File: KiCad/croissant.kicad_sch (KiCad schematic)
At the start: 53 parts, among them J1 USB_C_Receptacle_PowerOnly_6P, Q1 NMOS, SW1 SW_SPDT, U1 NE556, U2 TL064

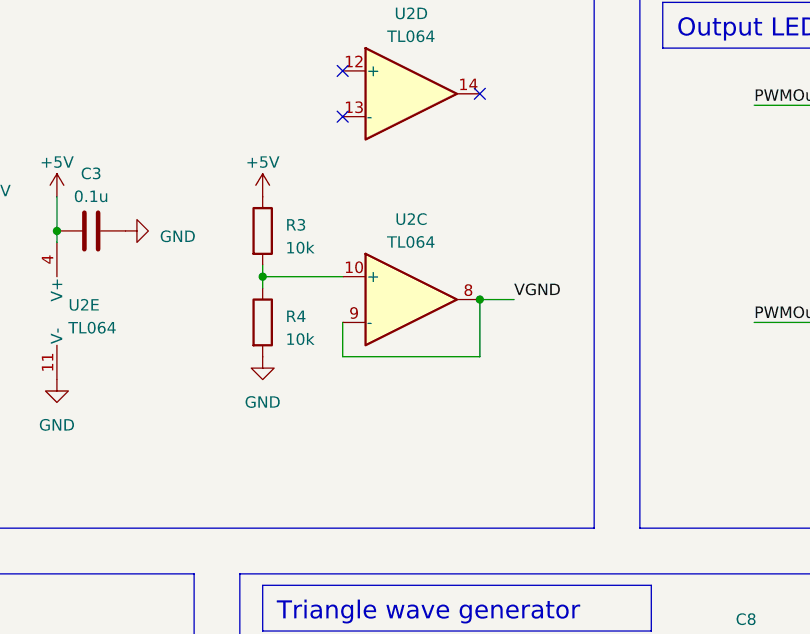
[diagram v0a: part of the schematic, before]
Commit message: Placed LEDs
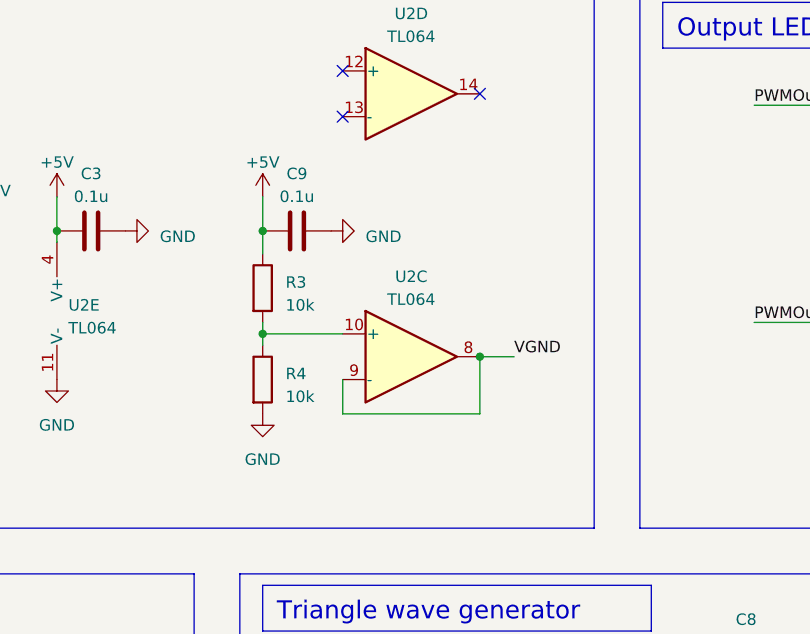
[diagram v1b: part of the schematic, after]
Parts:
- added C9: 0.1u, Capacitor_SMD:C_0603_1608Metric, symbol Device:C
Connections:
- net +5V: now also C9.1
- net GND: now also C9.2
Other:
- moved on the sheet: R3, R4, U2C
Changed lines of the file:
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@@
   (junction (at 63.5 132.08) (diameter 0) (color 0 0 0 0)
   )
-  (junction (at 133.35 66.04) (diameter 0) (color 0 0 0 0)
+  (junction (at 133.35 72.39) (diameter 0) (color 0 0 0 0)
   )
   (junction (at 261.62 105.41) (diameter 0) (color 0 0 0 0)
@@
   (junction (at 233.68 44.45) (diameter 0) (color 0 0 0 0)
   )
-  (junction (at 109.22 63.5) (diameter 0) (color 0 0 0 0)
+  (junction (at 109.22 69.85) (diameter 0) (color 0 0 0 0)
   )
   (junction (at 215.9 68.58) (diameter 0) (color 0 0 0 0)
@@
   )
   (junction (at 45.72 113.03) (diameter 0) (color 0 0 0 0)
+  )
+  (junction (at 109.22 58.42) (diameter 0) (color 0 0 0 0)
   )
   (junction (at 198.12 68.58) (diameter 0) (color 0 0 0 0)
@@
     (stroke (width 0) (type default))
   )
-  (wire (pts (xy 133.35 72.39) (xy 133.35 66.04))
+  (wire (pts (xy 133.35 78.74) (xy 133.35 72.39))
     (stroke (width 0) (type default))
   )
@@
     (stroke (width 0) (type default))
   )
-  (wire (pts (xy 109.22 63.5) (xy 118.11 63.5))
+  (wire (pts (xy 109.22 69.85) (xy 118.11 69.85))
     (stroke (width 0) (type default))
   )
@@
     (stroke (width 0) (type default))
   )
-  (wire (pts (xy 109.22 62.23) (xy 109.22 63.5))
+  (wire (pts (xy 109.22 58.42) (xy 109.22 54.61))
+    (stroke (width 0) (type default))
+  )
+  (wire (pts (xy 109.22 68.58) (xy 109.22 69.85))
     (stroke (width 0) (type default))
   )
@@
     (stroke (width 0) (type default))
   )
+  (wire (pts (xy 109.22 58.42) (xy 109.22 60.96))
+    (stroke (width 0) (type default))
+  )
   (wire (pts (xy 215.9 44.45) (xy 224.79 44.45))
     (stroke (width 0) (type default))
@@
     (stroke (width 0) (type default))
   )
-  (wire (pts (xy 109.22 63.5) (xy 109.22 64.77))
+  (wire (pts (xy 109.22 69.85) (xy 109.22 71.12))
     (stroke (width 0) (type default))
   )
@@
     (stroke (width 0) (type default))
   )
-  (wire (pts (xy 118.11 68.58) (xy 118.11 72.39))
+  (wire (pts (xy 118.11 74.93) (xy 118.11 78.74))
     (stroke (width 0) (type default))
   )
@@
     (stroke (width 0) (type default))
   )
-  (wire (pts (xy 118.11 72.39) (xy 133.35 72.39))
+  (wire (pts (xy 118.11 78.74) (xy 133.35 78.74))
     (stroke (width 0) (type default))
   )
@@
     (stroke (width 0) (type default))
   )
-  (wire (pts (xy 133.35 66.04) (xy 137.16 66.04))
+  (wire (pts (xy 133.35 72.39) (xy 137.16 72.39))
     (stroke (width 0) (type default))
   )
@@
     (effects (font (size 1.27 1.27)) (justify left bottom))
   )
-  (label "VGND" (at 137.16 66.04 0) (fields_autoplaced)
+  (label "VGND" (at 137.16 72.39 0) (fields_autoplaced)
     (effects (font (size 1.27 1.27)) (justify left bottom))
   )
@@
     )
   )
-  (symbol (lib_id "Device:R") (at 109.22 58.42 0) (unit 1)
-    (in_bom yes) (on_board yes) (dnp no) (fields_autoplaced)
-    (property "Reference" "R3" (at 111.76 57.785 0)
-      (effects (font (size 1.27 1.27)) (justify left))
-    )
-    (property "Value" "10k" (at 111.76 60.325 0)
-      (effects (font (size 1.27 1.27)) (justify left))
-    )
-    (property "Footprint" "Resistor_SMD:R_0603_1608Metric" (at 107.442 58.42 90)
-      (effects (font (size 1.27 1.27)) hide)
-    )
-    (property "Datasheet" "~" (at 109.22 58.42 0)
+  (symbol (lib_id "Device:R") (at 109.22 64.77 0) (unit 1)
+    (in_bom yes) (on_board yes) (dnp no) (fields_autoplaced)
+    (property "Reference" "R3" (at 111.76 64.135 0)
+      (effects (font (size 1.27 1.27)) (justify left))
+    )
+    (property "Value" "10k" (at 111.76 66.675 0)
+      (effects (font (size 1.27 1.27)) (justify left))
+    )
+    (property "Footprint" "Resistor_SMD:R_0603_1608Metric" (at 107.442 64.77 90)
+      (effects (font (size 1.27 1.27)) hide)
+    )
+    (property "Datasheet" "~" (at 109.22 64.77 0)
       (effects (font (size 1.27 1.27)) hide)
     )
@@
     )
   )
-  (symbol (lib_id "Device:R") (at 109.22 68.58 0) (unit 1)
-    (in_bom yes) (on_board yes) (dnp no) (fields_autoplaced)
-    (property "Reference" "R4" (at 111.76 67.945 0)
-      (effects (font (size 1.27 1.27)) (justify left))
-    )
-    (property "Value" "10k" (at 111.76 70.485 0)
-      (effects (font (size 1.27 1.27)) (justify left))
-    )
-    (property "Footprint" "Resistor_SMD:R_0603_1608Metric" (at 107.442 68.58 90)
-      (effects (font (size 1.27 1.27)) hide)
-    )
-    (property "Datasheet" "~" (at 109.22 68.58 0)
+  (symbol (lib_id "Device:R") (at 109.22 74.93 0) (unit 1)
+    (in_bom yes) (on_board yes) (dnp no) (fields_autoplaced)
+    (property "Reference" "R4" (at 111.76 74.295 0)
+      (effects (font (size 1.27 1.27)) (justify left))
+    )
+    (property "Value" "10k" (at 111.76 76.835 0)
+      (effects (font (size 1.27 1.27)) (justify left))
+    )
+    (property "Footprint" "Resistor_SMD:R_0603_1608Metric" (at 107.442 74.93 90)
+      (effects (font (size 1.27 1.27)) hide)
+    )
+    (property "Datasheet" "~" (at 109.22 74.93 0)
       (effects (font (size 1.27 1.27)) hide)
     )
@@
     )
   )
-  (symbol (lib_id "power:GND") (at 109.22 72.39 0) (unit 1)
-    (in_bom yes) (on_board yes) (dnp no) (fields_autoplaced)
-    (property "Reference" "#PWR016" (at 109.22 78.74 0)
-      (effects (font (size 1.27 1.27)) hide)
-    )
-    (property "Value" "GND" (at 109.22 77.47 0)
-      (effects (font (size 1.27 1.27)))
-    )
-    (property "Footprint" "" (at 109.22 72.39 0)
-      (effects (font (size 1.27 1.27)) hide)
-    )
-    (property "Datasheet" "" (at 109.22 72.39 0)
+  (symbol (lib_id "power:GND") (at 109.22 78.74 0) (unit 1)
+    (in_bom yes) (on_board yes) (dnp no) (fields_autoplaced)
+    (property "Reference" "#PWR016" (at 109.22 85.09 0)
+      (effects (font (size 1.27 1.27)) hide)
+    )
+    (property "Value" "GND" (at 109.22 83.82 0)
+      (effects (font (size 1.27 1.27)))
+    )
+    (property "Footprint" "" (at 109.22 78.74 0)
+      (effects (font (size 1.27 1.27)) hide)
+    )
+    (property "Datasheet" "" (at 109.22 78.74 0)
       (effects (font (size 1.27 1.27)) hide)
     )
@@
     )
   )
+  (symbol (lib_id "Device:C") (at 113.03 58.42 90) (unit 1)
+    (in_bom yes) (on_board yes) (dnp no) (fields_autoplaced)
+    (property "Reference" "C9" (at 113.03 52.07 90)
+      (effects (font (size 1.27 1.27)))
+    )
+    (property "Value" "0.1u" (at 113.03 54.61 90)
+      (effects (font (size 1.27 1.27)))
+    )
+    (property "Footprint" "Capacitor_SMD:C_0603_1608Metric" (at 116.84 57.4548 0)
+      (effects (font (size 1.27 1.27)) hide)
+    )
+    (property "Datasheet" "~" (at 113.03 58.42 0)
+      (effects (font (size 1.27 1.27)) hide)
+    )
+    (pin "1")
+    (pin "2")
+    (instances
+      (project "croissant"
+        (path "/9d4c4425-9345-4751-a711-72e95f2cc96d"
+          (reference "C9") (unit 1)
+        )
+      )
+    )
+  )
   (symbol (lib_id "power:PWR_FLAG") (at 71.12 53.34 0) (unit 1)
     (in_bom yes) (on_board yes) (dnp no) (fields_autoplaced)
@@
     )
   )
-  (symbol (lib_id "Amplifier_Operational:TL064") (at 125.73 66.04 0) (unit 3)
-    (in_bom yes) (on_board yes) (dnp no) (fields_autoplaced)
-    (property "Reference" "U2" (at 125.73 57.15 0)
-      (effects (font (size 1.27 1.27)))
-    )
-    (property "Value" "TL064" (at 125.73 59.69 0)
-      (effects (font (size 1.27 1.27)))
-    )
-    (property "Footprint" "Package_SO:SOIC-14_3.9x8.7mm_P1.27mm" (at 124.46 63.5 0)
-      (effects (font (size 1.27 1.27)) hide)
-    )
-    (property "Datasheet" "http://www.ti.com/lit/ds/symlink/tl061.pdf" (at 127 60.96 0)
+  (symbol (lib_id "Amplifier_Operational:TL064") (at 125.73 72.39 0) (unit 3)
+    (in_bom yes) (on_board yes) (dnp no) (fields_autoplaced)
+    (property "Reference" "U2" (at 125.73 63.5 0)
+      (effects (font (size 1.27 1.27)))
+    )
+    (property "Value" "TL064" (at 125.73 66.04 0)
+      (effects (font (size 1.27 1.27)))
+    )
+    (property "Footprint" "Package_SO:SOIC-14_3.9x8.7mm_P1.27mm" (at 124.46 69.85 0)
+      (effects (font (size 1.27 1.27)) hide)
+    )
+    (property "Datasheet" "http://www.ti.com/lit/ds/symlink/tl061.pdf" (at 127 67.31 0)
       (effects (font (size 1.27 1.27)) hide)
     )
@@
         )
       )
+    )
+  )
+  (symbol (lib_id "power:GND") (at 116.84 58.42 90) (unit 1)
+    (in_bom yes) (on_board yes) (dnp no) (fields_autoplaced)
+    (property "Reference" "#PWR039" (at 123.19 58.42 0)
+      (effects (font (size 1.27 1.27)) hide)
+    )
+    (property "Value" "GND" (at 120.65 59.055 90)
+      (effects (font (size 1.27 1.27)) (justify right))
+    )
+    (property "Footprint" "" (at 116.84 58.42 0)
+      (effects (font (size 1.27 1.27)) hide)
+    )
+    (property "Datasheet" "" (at 116.84 58.42 0)
+      (effects (font (size 1.27 1.27)) hide)
+    )
+    (pin "1")
+    (instances
+      (project "croissant"
+        (path "/9d4c4425-9345-4751-a711-72e95f2cc96d"
+          (reference "#PWR039") (unit 1)
+        )
+      )

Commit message: Fix LEDs silkscreen
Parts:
- D1, D10, D11, D12, D13, D14, D15, D2, D3, D4, D5, D6, D7, D8, D9: footprint LED_SMD:LED_0603_1608Metric -> croissant:LED_0603_NOSILK
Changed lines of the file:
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@@
       (effects (font (size 1.27 1.27)) (justify right))
     )
-    (property "Footprint" "LED_SMD:LED_0603_1608Metric" (at 215.9 80.01 0)
+    (property "Footprint" "croissant:LED_0603_NOSILK" (at 215.9 80.01 0)
       (effects (font (size 1.27 1.27)) hide)
     )
@@
       (effects (font (size 1.27 1.27)) (justify right))
     )
-    (property "Footprint" "LED_SMD:LED_0603_1608Metric" (at 215.9 55.88 0)
+    (property "Footprint" "croissant:LED_0603_NOSILK" (at 215.9 55.88 0)
       (effects (font (size 1.27 1.27)) hide)
     )
@@
       (effects (font (size 1.27 1.27)) (justify right))
     )
-    (property "Footprint" "LED_SMD:LED_0603_1608Metric" (at 198.12 55.88 0)
+    (property "Footprint" "croissant:LED_0603_NOSILK" (at 198.12 55.88 0)
       (effects (font (size 1.27 1.27)) hide)
     )
@@
       (effects (font (size 1.27 1.27)) (justify right))
     )
-    (property "Footprint" "LED_SMD:LED_0603_1608Metric" (at 224.79 55.88 0)
+    (property "Footprint" "croissant:LED_0603_NOSILK" (at 224.79 55.88 0)
       (effects (font (size 1.27 1.27)) hide)
     )
@@
       (effects (font (size 1.27 1.27)) (justify right))
     )
-    (property "Footprint" "LED_SMD:LED_0603_1608Metric" (at 207.01 55.88 0)
+    (property "Footprint" "croissant:LED_0603_NOSILK" (at 207.01 55.88 0)
       (effects (font (size 1.27 1.27)) hide)
     )
@@
       (effects (font (size 1.27 1.27)) (justify right))
     )
-    (property "Footprint" "LED_SMD:LED_0603_1608Metric" (at 233.68 80.01 0)
+    (property "Footprint" "croissant:LED_0603_NOSILK" (at 233.68 80.01 0)
       (effects (font (size 1.27 1.27)) hide)
     )
@@
       (effects (font (size 1.27 1.27)) (justify right))
     )
-    (property "Footprint" "LED_SMD:LED_0603_1608Metric" (at 198.12 80.01 0)
+    (property "Footprint" "croissant:LED_0603_NOSILK" (at 198.12 80.01 0)
       (effects (font (size 1.27 1.27)) hide)
     )
@@
       (effects (font (size 1.27 1.27)) (justify right))
     )
-    (property "Footprint" "LED_SMD:LED_0603_1608Metric" (at 207.01 80.01 0)
+    (property "Footprint" "croissant:LED_0603_NOSILK" (at 207.01 80.01 0)
       (effects (font (size 1.27 1.27)) hide)
     )
@@
       (effects (font (size 1.27 1.27)) (justify right))
     )
-    (property "Footprint" "LED_SMD:LED_0603_1608Metric" (at 242.57 55.88 0)
+    (property "Footprint" "croissant:LED_0603_NOSILK" (at 242.57 55.88 0)
       (effects (font (size 1.27 1.27)) hide)
     )
@@
       (effects (font (size 1.27 1.27)) (justify right))
     )
-    (property "Footprint" "LED_SMD:LED_0603_1608Metric" (at 224.79 80.01 0)
+    (property "Footprint" "croissant:LED_0603_NOSILK" (at 224.79 80.01 0)
       (effects (font (size 1.27 1.27)) hide)
     )
@@
       (effects (font (size 1.27 1.27)) (justify right))
     )
-    (property "Footprint" "LED_SMD:LED_0603_1608Metric" (at 180.34 55.88 0)
+    (property "Footprint" "croissant:LED_0603_NOSILK" (at 180.34 55.88 0)
       (effects (font (size 1.27 1.27)) hide)
     )
@@
       (effects (font (size 1.27 1.27)) (justify right))
     )
-    (property "Footprint" "LED_SMD:LED_0603_1608Metric" (at 233.68 55.88 0)
+    (property "Footprint" "croissant:LED_0603_NOSILK" (at 233.68 55.88 0)
       (effects (font (size 1.27 1.27)) hide)
     )
@@
       (effects (font (size 1.27 1.27)) (justify right))
     )
-    (property "Footprint" "LED_SMD:LED_0603_1608Metric" (at 189.23 80.01 0)
+    (property "Footprint" "croissant:LED_0603_NOSILK" (at 189.23 80.01 0)
       (effects (font (size 1.27 1.27)) hide)
     )
@@
       (effects (font (size 1.27 1.27)) (justify right))
     )
-    (property "Footprint" "LED_SMD:LED_0603_1608Metric" (at 189.23 55.88 0)
+    (property "Footprint" "croissant:LED_0603_NOSILK" (at 189.23 55.88 0)
       (effects (font (size 1.27 1.27)) hide)
     )
@@
       (effects (font (size 1.27 1.27)) (justify right))
     )
-    (property "Footprint" "LED_SMD:LED_0603_1608Metric" (at 180.34 80.01 0)
-      (effects (font (size 1.27 1.27)) hide)
-    )
+    (property "Footprint" "croissant:LED_0603_NOSILK" (at 180.34 80.01 0)
+      (effects (font (size 1.27 1.27)) hide)
+    )
